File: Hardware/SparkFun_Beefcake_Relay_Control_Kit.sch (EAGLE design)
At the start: 17 parts, among them K1 JQX-15F, Q1 2N3904

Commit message: updated designators
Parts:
- renumbered R3 to R1
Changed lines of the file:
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@@
 <attribute name="PROD_ID" value="DIO-09529"/>
 </part>
-<part name="R3" library="SparkFun-Resistors" deviceset="1KOHM-1/4W-1%(PTH)" device="HORIZ-KIT" value="1K"/>
+<part name="R1" library="SparkFun-Resistors" deviceset="1KOHM-1/4W-1%(PTH)" device="HORIZ-KIT" value="1K"/>
 <part name="U$3" library="SparkFun" deviceset="STAND-OFF" device=""/>
 <part name="U$4" library="SparkFun" deviceset="STAND-OFF" device=""/>
@@
 <attribute name="VALUE" x="140.335" y="84.328" size="1.778" layer="96" rot="R90"/>
 </instance>
-<instance part="R3" gate="G$1" x="134.62" y="76.2" rot="R90"/>
+<instance part="R1" gate="G$1" x="134.62" y="76.2" rot="R90"/>
 <instance part="U$3" gate="G$1" x="246.38" y="25.4"/>
 <instance part="U$4" gate="G$1" x="241.3" y="25.4"/>
@@
 <wire x1="134.62" y1="81.28" x2="134.62" y2="83.82" width="0.1524" layer="91"/>
 <pinref part="LED1" gate="G$1" pin="C"/>
-<pinref part="R3" gate="G$1" pin="2"/>
+<pinref part="R1" gate="G$1" pin="2"/>
 </segment>
 </net>
@@
 <label x="112.268" y="120.142" size="1.778" layer="95"/>
 <pinref part="Q1" gate="G$1" pin="C"/>
-<pinref part="R3" gate="G$1" pin="1"/>
+<pinref part="R1" gate="G$1" pin="1"/>
 <wire x1="106.68" y1="58.42" x2="106.68" y2="68.58" width="0.1524" layer="91"/>
 <wire x1="106.68" y1="68.58" x2="106.68" y2="119.38" width="0.1524" layer="91"/>

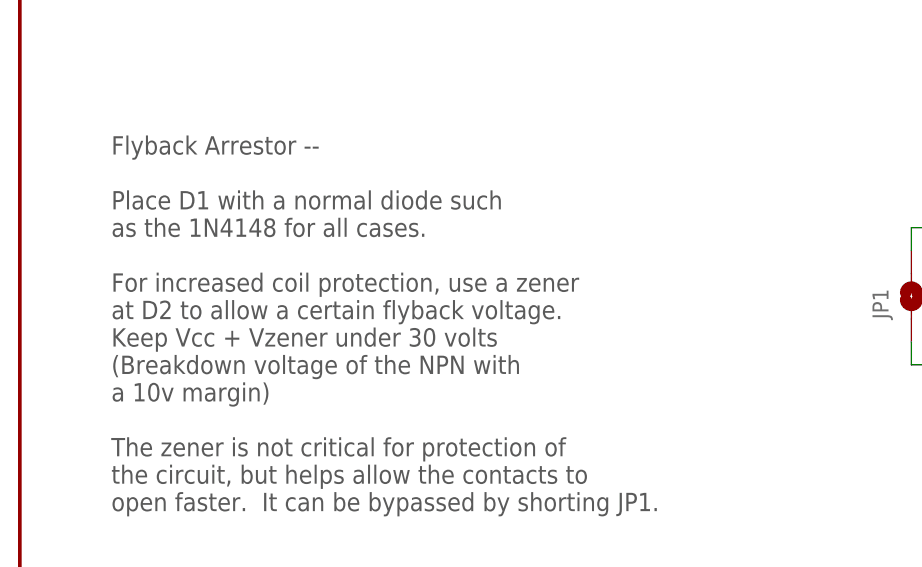
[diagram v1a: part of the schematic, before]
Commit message: Pointed pictures and links to new product listing, preparing for merge, fixed typo in schematic text
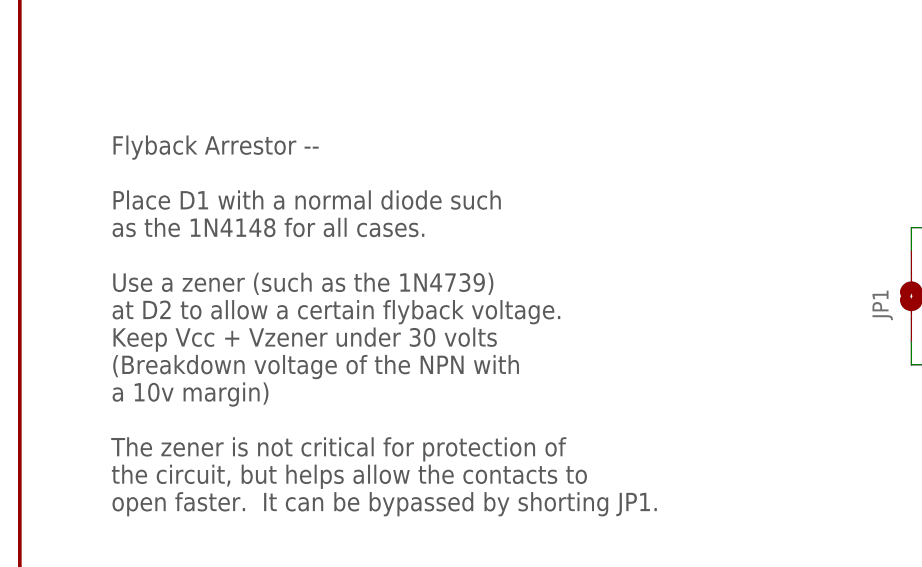
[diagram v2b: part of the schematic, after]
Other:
- note added: "Flyback Arrestor -- Place D1 with a normal diode such as the 1N4148 for all cases. Use a zener (such as the 1N4739) at D2 to allow a certain flyback voltage. Keep Vcc + Vzener under 30 volts (Breakdown voltage of the NPN with a 10v margin) The zener is not critical for protection of the circuit, but helps allow the contacts to open faster. It can be bypassed by shorting JP1."
- note removed: "Flyback Arrestor -- Place D1 with a normal diode such as the 1N4148 for all cases. For increased coil protection, use a zener at D2 to allow a certain flyback voltage. Keep Vcc + Vzener under 30 volts (Breakdown voltage of the NPN with a 10v margin) The zener is not critical for protection of the circuit, but helps allow the contacts to open faster. It can be bypassed by shorting JP1."
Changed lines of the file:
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@@
 Place D1 with a normal diode such
 as the 1N4148 for all cases.
-For increased coil protection, use a zener
+Use a zener (such as the 1N4739)
 at D2 to allow a certain flyback voltage.
 Keep Vcc + Vzener under 30 volts
